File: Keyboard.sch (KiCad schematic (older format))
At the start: 1 part

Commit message: 3 Board Schematics Complete
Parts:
- added J?: SOLDER_PAD_CONNECTION, symbol Connector_Generic:Conn_02x14_Odd_Even
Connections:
- net CKEYS_4_OUT: now reaches J?.10 (Pin_10)
- net CKEYS_RCLK: now reaches J?.18 (Pin_18)
- net CKEYS_RCLK: now also J?.25 (Pin_25)
- net CKEYS_0_OUT: now reaches J?.2 (Pin_2)
- net CKEYS_CLK: now reaches J?.20 (Pin_20)
- net CKEYS_CLK: now also J?.23 (Pin_23)
- net CKEYS_RES: now reaches J?.22 (Pin_22)
- net CKEYS_RES: now also J?.21 (Pin_21)
- net CKEYS_DIM: now reaches J?.24 (Pin_24)
- net CKEYS_DIM: now also J?.19 (Pin_19)
- net CKEYS_3.3V: now reaches J?.26 (Pin_26)
- net CKEYS_3.3V: now also J?.17 (Pin_17)
- net CKEYS_GND: now reaches J?.28 (Pin_28)
- net CKEYS_GND: now also J?.27 (Pin_27)
- net CKEYS_1_OUT: now reaches J?.4 (Pin_4)
- net CKEYS_2_OUT: now reaches J?.6 (Pin_6)
- net CKEYS_3_OUT: now reaches J?.8 (Pin_8)
- new net CKEYS_0_IN: J?.1 (Pin_1)
- new net CKEYS_1_IN: J?.3 (Pin_3)
- new net LMK/3.3V: J?.18 (Pin_18)
- new net LMK/DIMMER: J?.20 (Pin_20)
- new net LMK/GND: J?.28 (Pin_28)
- new net LMK/RESET: J?.22 (Pin_22)
- new net LMK/SHIFT_0_DATA: J?.2 (Pin_2)
- new net LMK/SHIFT_1_DATA: J?.4 (Pin_4)
- new net LMK/SHIFT_CLK: J?.24 (Pin_24)
- new net LMK/SHIFT_RCLK: J?.26 (Pin_26)
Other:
- moved on the sheet: J?

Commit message: Schematic completed first draft
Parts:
- added J? (x3): SOLDER_PAD_CONNECTION, symbol Connector_Generic:Conn_02x14_Odd_Even
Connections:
- net LMK/DIMMER is gone; now on net RKEYS_3.3V: J?.20 (Pin_20)
- net CKEYS_3.3V: now also J?.17 (Pin_17)
- net CKEYS_3_IN: now also J?.1 (Pin_1)
- net CKEYS_4_IN: now also J?.3 (Pin_3)
- net CKEYS_CLK: now also J?.23 (Pin_23)
- net CKEYS_DIM: now also J?.19 (Pin_19)
- net CKEYS_GND: now also J?.27 (Pin_27)
- net CKEYS_RCLK: now also J?.25 (Pin_25)
- net CKEYS_RES: now also J?.21 (Pin_21)
- net LMK/SHIFT_0_DATA_IN: now also J?.1 (Pin_1)
- net LMK/3.3V renamed RKEYS_3.3V
- net RKEYS_3.3V: now also J?.17 (Pin_17), J?.17 (Pin_17), J?.18 (Pin_18), J?.19 (Pin_19), J?.19 (Pin_19), J?.20 (Pin_20)
- net LMK/GND renamed RKEYS_GND
- net RKEYS_GND: now also J?.27 (Pin_27), J?.27 (Pin_27), J?.28 (Pin_28)
- net LMK/RESET renamed RKEYS_RES
- net RKEYS_RES: now also J?.21 (Pin_21), J?.21 (Pin_21), J?.22 (Pin_22)
- net LMK/SHIFT_0_DATA renamed RKEYS_0_OUT
- net LMK/SHIFT_1_DATA renamed RKEYS_1_OUT
- net LMK/SHIFT_CLK renamed RKEYS_CLK
- net RKEYS_CLK: now also J?.23 (Pin_23), J?.23 (Pin_23), J?.24 (Pin_24)
- net LMK/SHIFT_RCLK renamed RKEYS_RCLK
- net RKEYS_RCLK: now also J?.25 (Pin_25), J?.25 (Pin_25), J?.26 (Pin_26)
- new net CK/SHIFT_4_DATA: J?.2 (Pin_2)
- new net CTKEYS_3.3V: J?.18 (Pin_18)
- new net CTKEYS_CLK: J?.24 (Pin_24)
- new net CTKEYS_DIM: J?.20 (Pin_20)
- new net CTKEYS_GND: J?.28 (Pin_28)
- new net CTKEYS_RCLK: J?.26 (Pin_26)
- new net CTKEYS_RES: J?.22 (Pin_22)
- new net NKEYS_3.3V: J?.18 (Pin_18)
- new net NKEYS_CLK: J?.24 (Pin_24)
- new net NKEYS_DIM: J?.20 (Pin_20)
- new net NKEYS_GND: J?.28 (Pin_28)
- new net NKEYS_RCLK: J?.26 (Pin_26)
- new net NKEYS_RES: J?.22 (Pin_22)
- new net Num/SHIFT_0_DATA: J?.2 (Pin_2)
- new net RMK/SHIFT_3_DATA: J?.2 (Pin_2)
- new net RMK/SHIFT_4_DATA: J?.4 (Pin_4)
- new net RMK/SHIFT_4_DATA_IN: J?.1 (Pin_1)

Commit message: Fixed PISO Shift Register Wiring
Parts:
- J? (x5): footprint (none) -> Solder Pad Connections:Solder_Pad_Bridge_Connections
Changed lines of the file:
@@
 F 0 "J?" V 8204 1962 50  0000 R CNN
 F 1 "SOLDER_PAD_CONNECTION" V 8295 1962 50  0000 R CNN
-F 2 "" H 8200 2750 50  0001 C CNN
+F 2 "Solder Pad Connections:Solder_Pad_Bridge_Connections" H 8200 2750 50  0001 C CNN
 F 3 "~" H 8200 2750 50  0001 C CNN
 	1    8200 2750
@@
 F 0 "J?" V 5954 6112 50  0000 R CNN
 F 1 "SOLDER_PAD_CONNECTION" V 6045 6112 50  0000 R CNN
-F 2 "" H 5950 6900 50  0001 C CNN
+F 2 "Solder Pad Connections:Solder_Pad_Bridge_Connections" H 5950 6900 50  0001 C CNN
 F 3 "~" H 5950 6900 50  0001 C CNN
 	1    5950 6900
@@
 F 0 "J?" V 10054 6112 50  0000 R CNN
 F 1 "SOLDER_PAD_CONNECTION" V 10145 6112 50  0000 R CNN
-F 2 "" H 10050 6900 50  0001 C CNN
+F 2 "Solder Pad Connections:Solder_Pad_Bridge_Connections" H 10050 6900 50  0001 C CNN
 F 3 "~" H 10050 6900 50  0001 C CNN
 	1    10050 6900
@@
 F 0 "J?" V 1554 4962 50  0000 R CNN
 F 1 "SOLDER_PAD_CONNECTION" V 1645 4962 50  0000 R CNN
-F 2 "" H 1550 5750 50  0001 C CNN
+F 2 "Solder Pad Connections:Solder_Pad_Bridge_Connections" H 1550 5750 50  0001 C CNN
 F 3 "~" H 1550 5750 50  0001 C CNN
 	1    1550 5750
@@
 F 0 "J?" V 14754 4962 50  0000 R CNN
 F 1 "SOLDER_PAD_CONNECTION" V 14845 4962 50  0000 R CNN
-F 2 "" H 14750 5750 50  0001 C CNN
+F 2 "Solder Pad Connections:Solder_Pad_Bridge_Connections" H 14750 5750 50  0001 C CNN
 F 3 "~" H 14750 5750 50  0001 C CNN
 	1    14750 5750

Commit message: Corrected errors found in design rule check
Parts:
- gave numbers to parts that had none: 5
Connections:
- no-connect marks 0 -> 59
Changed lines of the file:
@@
 $EndSheet
 $Comp
-L Connector_Generic:Conn_02x14_Odd_Even J?
+L Connector_Generic:Conn_02x14_Odd_Even J1
 U 1 1 5EBFED5A
 P 8200 2750
-F 0 "J?" V 8204 1962 50  0000 R CNN
+F 0 "J1" V 8204 1962 50  0000 R CNN
 F 1 "SOLDER_PAD_CONNECTION" V 8295 1962 50  0000 R CNN
 F 2 "Solder Pad Connections:Solder_Pad_Bridge_Connections" H 8200 2750 50  0001 C CNN
@@
 $EndSheet
 $Comp
-L Connector_Generic:Conn_02x14_Odd_Even J?
+L Connector_Generic:Conn_02x14_Odd_Even J4
 U 1 1 5EB88EB0
 P 5950 6900
-F 0 "J?" V 5954 6112 50  0000 R CNN
+F 0 "J4" V 5954 6112 50  0000 R CNN
 F 1 "SOLDER_PAD_CONNECTION" V 6045 6112 50  0000 R CNN
 F 2 "Solder Pad Connections:Solder_Pad_Bridge_Connections" H 5950 6900 50  0001 C CNN
@@
 $EndSheet
 $Comp
-L Connector_Generic:Conn_02x14_Odd_Even J?
+L Connector_Generic:Conn_02x14_Odd_Even J5
 U 1 1 5F364499
 P 10050 6900
-F 0 "J?" V 10054 6112 50  0000 R CNN
+F 0 "J5" V 10054 6112 50  0000 R CNN
 F 1 "SOLDER_PAD_CONNECTION" V 10145 6112 50  0000 R CNN
 F 2 "Solder Pad Connections:Solder_Pad_Bridge_Connections" H 10050 6900 50  0001 C CNN
@@
 	9300 6500 6700 6500
 $Comp
-L Connector_Generic:Conn_02x14_Odd_Even J?
+L Connector_Generic:Conn_02x14_Odd_Even J2
 U 1 1 5F3CAD0C
 P 1550 5750
-F 0 "J?" V 1554 4962 50  0000 R CNN
+F 0 "J2" V 1554 4962 50  0000 R CNN
 F 1 "SOLDER_PAD_CONNECTION" V 1645 4962 50  0000 R CNN
 F 2 "Solder Pad Connections:Solder_Pad_Bridge_Connections" H 1550 5750 50  0001 C CNN
@@
 	10550 6400 10350 6400
 $Comp
-L Connector_Generic:Conn_02x14_Odd_Even J?
+L Connector_Generic:Conn_02x14_Odd_Even J3
 U 1 1 6019F7ED
 P 14750 5750
-F 0 "J?" V 14754 4962 50  0000 R CNN
+F 0 "J3" V 14754 4962 50  0000 R CNN
 F 1 "SOLDER_PAD_CONNECTION" V 14845 4962 50  0000 R CNN
 F 2 "Solder Pad Connections:Solder_Pad_Bridge_Connections" H 14750 5750 50  0001 C CNN
@@
 Wire Bus Line
 	14850 3500 14850 4800
+NoConn ~ 14850 5950
+NoConn ~ 14750 5950
+NoConn ~ 14650 5950
+NoConn ~ 14550 5950
+NoConn ~ 14450 5950
+NoConn ~ 14350 5950
+NoConn ~ 14250 5950
+NoConn ~ 14250 5450
+NoConn ~ 14350 5450
+NoConn ~ 14450 5450
+NoConn ~ 14550 5450
+NoConn ~ 14650 5450
+NoConn ~ 14750 5450
+NoConn ~ 14850 5450
+NoConn ~ 8100 3050
+NoConn ~ 8200 3050
+NoConn ~ 8300 3050
+NoConn ~ 8300 2550
+NoConn ~ 8200 2550
+NoConn ~ 10350 6500
+NoConn ~ 10350 6600
+NoConn ~ 10350 6700
+NoConn ~ 10350 6800
+NoConn ~ 10350 6900
+NoConn ~ 10350 7000
+NoConn ~ 9850 7000
+NoConn ~ 9850 6900
+NoConn ~ 9850 6800
+NoConn ~ 9850 6700
+NoConn ~ 9850 6600
+NoConn ~ 9850 6500
+NoConn ~ 6150 7000
+NoConn ~ 6150 6900
+NoConn ~ 6150 6800
+NoConn ~ 6150 6700
+NoConn ~ 6150 6600
+NoConn ~ 6150 6500
+NoConn ~ 5650 6500
+NoConn ~ 5650 6600
+NoConn ~ 5650 6700
+NoConn ~ 5650 6800
+NoConn ~ 5650 6900
+NoConn ~ 5650 7000
+NoConn ~ 1650 5950
+NoConn ~ 1650 5450
+NoConn ~ 1550 5450
+NoConn ~ 1550 5950
+NoConn ~ 1450 5950
+NoConn ~ 1450 5450
+NoConn ~ 1350 5450
+NoConn ~ 1250 5450
+NoConn ~ 1150 5450
+NoConn ~ 1050 5450
+NoConn ~ 1050 5950
+NoConn ~ 1150 5950
+NoConn ~ 1250 5950
+Text Label 11600 3800 2    50   ~ 0
+CTKEYS_3.3V
+Text Label 11600 3900 2    50   ~ 0
+CTKEYS_DIM
+Text Label 11600 4000 2    50   ~ 0
+CTKEYS_RES
+Text Label 11600 4100 2    50   ~ 0
+CTKEYS_CLK
+Text Label 11600 4200 2    50   ~ 0
+CTKEYS_RCLK
+Text Label 11600 4300 2    50   ~ 0
+CTKEYS_GND
+NoConn ~ 1350 5950
+NoConn ~ 7500 5650
+NoConn ~ 9000 5000
 Wire Bus Line
 	2400 6400 2400 6700

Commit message: Redesigned for single large PCB
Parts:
- removed J1, J2, J3, J4, J5: SOLDER_PAD_CONNECTION, Solder Pad Connections:Solder_Pad_Bridge_Connections, symbol Connector_Generic:Conn_02x14_Odd_Even
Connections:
- no-connect marks 59 -> 0

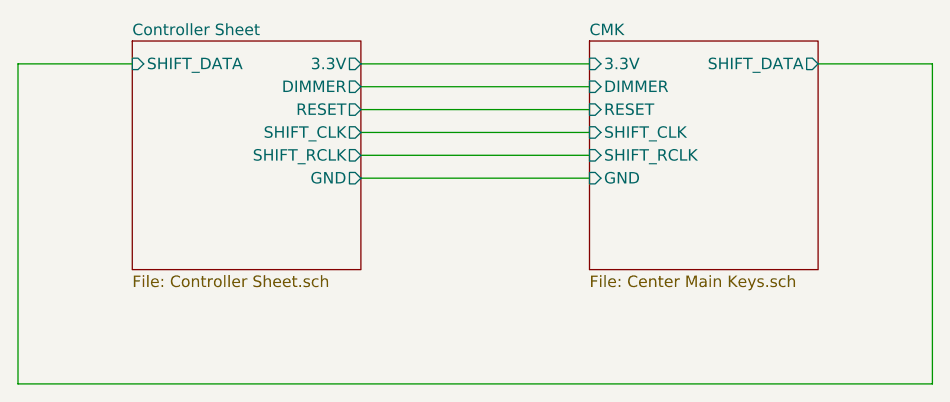
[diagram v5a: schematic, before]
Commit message: PCB Routed, minor circuit changes
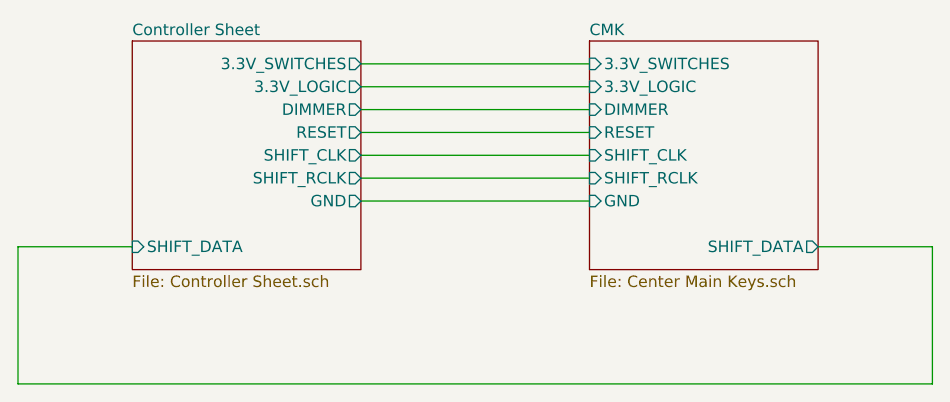
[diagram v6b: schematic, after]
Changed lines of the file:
@@
 F0 "Controller Sheet" 50
 F1 "Controller Sheet.sch" 50
-F2 "RESET" O R 5000 3700 50
-F3 "SHIFT_RCLK" O R 5000 3900 50
-F4 "SHIFT_CLK" O R 5000 3800 50
-F5 "3.3V" O R 5000 3500 50
-F6 "GND" O R 5000 4000 50
-F7 "DIMMER" O R 5000 3600 50
-F8 "SHIFT_DATA" I L 4000 3500 50
+F2 "RESET" O R 5000 3800 50
+F3 "SHIFT_RCLK" O R 5000 4000 50
+F4 "SHIFT_CLK" O R 5000 3900 50
+F5 "GND" O R 5000 4100 50
+F6 "DIMMER" O R 5000 3700 50
+F7 "SHIFT_DATA" I L 4000 4300 50
+F8 "3.3V_LOGIC" O R 5000 3600 50
+F9 "3.3V_SWITCHES" O R 5000 3500 50
 $EndSheet
-Wire Wire Line
-	5000 3500 6000 3500
 Wire Wire Line
 	5000 3600 6000 3600
@@
 Wire Wire Line
 	5000 4000 6000 4000
+Wire Wire Line
+	5000 4100 6000 4100
 $Sheet
 S 6000 3400 1000 1000
@@
 F0 "CMK" 50
 F1 "Center Main Keys.sch" 50
-F2 "3.3V" I L 6000 3500 50
-F3 "DIMMER" I L 6000 3600 50
-F4 "RESET" I L 6000 3700 50
-F5 "SHIFT_CLK" I L 6000 3800 50
-F6 "SHIFT_RCLK" I L 6000 3900 50
-F7 "GND" I L 6000 4000 50
-F8 "SHIFT_DATA" O R 7000 3500 50
+F2 "DIMMER" I L 6000 3700 50
+F3 "RESET" I L 6000 3800 50
+F4 "SHIFT_CLK" I L 6000 3900 50
+F5 "SHIFT_RCLK" I L 6000 4000 50
+F6 "GND" I L 6000 4100 50
+F7 "SHIFT_DATA" O R 7000 4300 50
+F8 "3.3V_LOGIC" I L 6000 3600 50
+F9 "3.3V_SWITCHES" I L 6000 3500 50
 $EndSheet
-Wire Wire Line
-	4000 3500 3500 3500
 Wire Wire Line
 	3500 4900 7500 4900
 Wire Wire Line
-	7500 4900 7500 3500
+	3500 4900 3500 4300
 Wire Wire Line
-	7500 3500 7000 3500
+	3500 4300 4000 4300
 Wire Wire Line
-	3500 3500 3500 4900
+	7500 4900 7500 4300
+Wire Wire Line
+	7500 4300 7000 4300
+Wire Wire Line
+	5000 3500 6000 3500
 $EndSCHEMATC
